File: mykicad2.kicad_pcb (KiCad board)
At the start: 2 copper layers, 8 parts, among them Q1 MMBT3904, Q2 MMBT3906

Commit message: update
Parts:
- added P1: CONN_01X06, Pin_Headers:Pin_Header_Angled_1x06, F.Cu at (170.2, 92.7)
- moved R1 13.1 mm to (143.5, 95.2), turned to 270 degrees
- moved R2 9.16 mm to (143.5, 113.0)
- moved Q1 7.73 mm to (158.8, 95.2), turned to 0 degrees
- moved R3 5.24 mm to (160.0, 102.9), turned to 270 degrees
- moved R4 4.02 mm to (160.0, 108.0), turned to 270 degrees
- turned D1 to 270 degrees
- turned D2 to 270 degrees
- turned Q2 to 0 degrees

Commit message: vertical header pins
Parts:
- P1: footprint Pin_Headers:Pin_Header_Angled_1x06 -> Pin_Headers:Pin_Header_Straight_1x06
- moved D1 6.35 mm to (149.9, 101.6)
- moved D2 6.35 mm to (149.9, 108.0)
- moved R1 6.35 mm to (149.9, 95.2)
- moved R2 6.35 mm to (149.9, 113.0)
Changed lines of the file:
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@@
   )
   (module Diodes_SMD:MiniMELF_Standard (layer F.Cu)
-    (at 143.51 101.6 270)
+    (at 149.86 101.6 270)
     (descr "Diode Mini-MELF Standard")
     (tags "Diode Mini-MELF Standard")
@@
   )
   (module Diodes_SMD:MiniMELF_Standard (layer F.Cu)
-    (at 143.51 107.95 270)
+    (at 149.86 107.95 270)
     (descr "Diode Mini-MELF Standard")
     (tags "Diode Mini-MELF Standard")
@@
   )
   (module Resistors_SMD:R_0603 (layer F.Cu)
-    (at 143.51 95.25 270)
+    (at 149.86 95.25 270)
     (descr "Resistor SMD 0603, reflow soldering, Vishay (see dcrcw.pdf)")
     (tags "resistor 0603")
@@
   )
   (module Resistors_SMD:R_0603 (layer F.Cu)
-    (at 143.51 113.03 270)
+    (at 149.86 113.03 270)
     (descr "Resistor SMD 0603, reflow soldering, Vishay (see dcrcw.pdf)")
     (tags "resistor 0603")
@@
     )
   )
-  (module Pin_Headers:Pin_Header_Angled_1x06 (layer F.Cu)
+  (module Pin_Headers:Pin_Header_Straight_1x06 (layer F.Cu)
     (at 170.18 92.71)
     (descr "Through hole pin header")
@@
       (effects (font (size 1 1) (thickness 0.15)))
     )
-    (fp_line (start -1.5 -1.75) (end -1.5 14.45) (layer F.CrtYd) (width 0.05))
-    (fp_line (start 10.65 -1.75) (end 10.65 14.45) (layer F.CrtYd) (width 0.05))
-    (fp_line (start -1.5 -1.75) (end 10.65 -1.75) (layer F.CrtYd) (width 0.05))
-    (fp_line (start -1.5 14.45) (end 10.65 14.45) (layer F.CrtYd) (width 0.05))
-    (fp_line (start -1.3 -1.55) (end -1.3 0) (layer F.SilkS) (width 0.15))
-    (fp_line (start 0 -1.55) (end -1.3 -1.55) (layer F.SilkS) (width 0.15))
-    (fp_line (start 4.191 -0.127) (end 10.033 -0.127) (layer F.SilkS) (width 0.15))
-    (fp_line (start 10.033 -0.127) (end 10.033 0.127) (layer F.SilkS) (width 0.15))
-    (fp_line (start 10.033 0.127) (end 4.191 0.127) (layer F.SilkS) (width 0.15))
-    (fp_line (start 4.191 0.127) (end 4.191 0) (layer F.SilkS) (width 0.15))
-    (fp_line (start 4.191 0) (end 10.033 0) (layer F.SilkS) (width 0.15))
-    (fp_line (start 1.524 -0.254) (end 1.143 -0.254) (layer F.SilkS) (width 0.15))
-    (fp_line (start 1.524 0.254) (end 1.143 0.254) (layer F.SilkS) (width 0.15))
-    (fp_line (start 1.524 2.286) (end 1.143 2.286) (layer F.SilkS) (width 0.15))
-    (fp_line (start 1.524 2.794) (end 1.143 2.794) (layer F.SilkS) (width 0.15))
-    (fp_line (start 1.524 4.826) (end 1.143 4.826) (layer F.SilkS) (width 0.15))
-    (fp_line (start 1.524 5.334) (end 1.143 5.334) (layer F.SilkS) (width 0.15))
-    (fp_line (start 1.524 12.954) (end 1.143 12.954) (layer F.SilkS) (width 0.15))
-    (fp_line (start 1.524 12.446) (end 1.143 12.446) (layer F.SilkS) (width 0.15))
-    (fp_line (start 1.524 10.414) (end 1.143 10.414) (layer F.SilkS) (width 0.15))
-    (fp_line (start 1.524 9.906) (end 1.143 9.906) (layer F.SilkS) (width 0.15))
-    (fp_line (start 1.524 7.874) (end 1.143 7.874) (layer F.SilkS) (width 0.15))
-    (fp_line (start 1.524 7.366) (end 1.143 7.366) (layer F.SilkS) (width 0.15))
-    (fp_line (start 1.524 -1.27) (end 4.064 -1.27) (layer F.SilkS) (width 0.15))
-    (fp_line (start 1.524 1.27) (end 4.064 1.27) (layer F.SilkS) (width 0.15))
-    (fp_line (start 1.524 1.27) (end 1.524 3.81) (layer F.SilkS) (width 0.15))
-    (fp_line (start 1.524 3.81) (end 4.064 3.81) (layer F.SilkS) (width 0.15))
-    (fp_line (start 4.064 2.286) (end 10.16 2.286) (layer F.SilkS) (width 0.15))
-    (fp_line (start 10.16 2.286) (end 10.16 2.794) (layer F.SilkS) (width 0.15))
-    (fp_line (start 10.16 2.794) (end 4.064 2.794) (layer F.SilkS) (width 0.15))
-    (fp_line (start 4.064 3.81) (end 4.064 1.27) (layer F.SilkS) (width 0.15))
-    (fp_line (start 4.064 1.27) (end 4.064 -1.27) (layer F.SilkS) (width 0.15))
-    (fp_line (start 10.16 0.254) (end 4.064 0.254) (layer F.SilkS) (width 0.15))
-    (fp_line (start 10.16 -0.254) (end 10.16 0.254) (layer F.SilkS) (width 0.15))
-    (fp_line (start 4.064 -0.254) (end 10.16 -0.254) (layer F.SilkS) (width 0.15))
-    (fp_line (start 1.524 1.27) (end 4.064 1.27) (layer F.SilkS) (width 0.15))
-    (fp_line (start 1.524 -1.27) (end 1.524 1.27) (layer F.SilkS) (width 0.15))
-    (fp_line (start 1.524 8.89) (end 4.064 8.89) (layer F.SilkS) (width 0.15))
-    (fp_line (start 1.524 8.89) (end 1.524 11.43) (layer F.SilkS) (width 0.15))
-    (fp_line (start 1.524 11.43) (end 4.064 11.43) (layer F.SilkS) (width 0.15))
-    (fp_line (start 4.064 9.906) (end 10.16 9.906) (layer F.SilkS) (width 0.15))
-    (fp_line (start 10.16 9.906) (end 10.16 10.414) (layer F.SilkS) (width 0.15))
-    (fp_line (start 10.16 10.414) (end 4.064 10.414) (layer F.SilkS) (width 0.15))
-    (fp_line (start 4.064 11.43) (end 4.064 8.89) (layer F.SilkS) (width 0.15))
-    (fp_line (start 4.064 13.97) (end 4.064 11.43) (layer F.SilkS) (width 0.15))
-    (fp_line (start 10.16 12.954) (end 4.064 12.954) (layer F.SilkS) (width 0.15))
-    (fp_line (start 10.16 12.446) (end 10.16 12.954) (layer F.SilkS) (width 0.15))
-    (fp_line (start 4.064 12.446) (end 10.16 12.446) (layer F.SilkS) (width 0.15))
-    (fp_line (start 1.524 13.97) (end 4.064 13.97) (layer F.SilkS) (width 0.15))
-    (fp_line (start 1.524 11.43) (end 1.524 13.97) (layer F.SilkS) (width 0.15))
-    (fp_line (start 1.524 11.43) (end 4.064 11.43) (layer F.SilkS) (width 0.15))
-    (fp_line (start 1.524 6.35) (end 4.064 6.35) (layer F.SilkS) (width 0.15))
-    (fp_line (start 1.524 6.35) (end 1.524 8.89) (layer F.SilkS) (width 0.15))
-    (fp_line (start 1.524 8.89) (end 4.064 8.89) (layer F.SilkS) (width 0.15))
-    (fp_line (start 4.064 7.366) (end 10.16 7.366) (layer F.SilkS) (width 0.15))
-    (fp_line (start 10.16 7.366) (end 10.16 7.874) (layer F.SilkS) (width 0.15))
-    (fp_line (start 10.16 7.874) (end 4.064 7.874) (layer F.SilkS) (width 0.15))
-    (fp_line (start 4.064 8.89) (end 4.064 6.35) (layer F.SilkS) (width 0.15))
-    (fp_line (start 4.064 6.35) (end 4.064 3.81) (layer F.SilkS) (width 0.15))
-    (fp_line (start 10.16 5.334) (end 4.064 5.334) (layer F.SilkS) (width 0.15))
-    (fp_line (start 10.16 4.826) (end 10.16 5.334) (layer F.SilkS) (width 0.15))
-    (fp_line (start 4.064 4.826) (end 10.16 4.826) (layer F.SilkS) (width 0.15))
-    (fp_line (start 1.524 6.35) (end 4.064 6.35) (layer F.SilkS) (width 0.15))
-    (fp_line (start 1.524 3.81) (end 1.524 6.35) (layer F.SilkS) (width 0.15))
-    (fp_line (start 1.524 3.81) (end 4.064 3.81) (layer F.SilkS) (width 0.15))
+    (fp_line (start -1.75 -1.75) (end -1.75 14.45) (layer F.CrtYd) (width 0.05))
+    (fp_line (start 1.75 -1.75) (end 1.75 14.45) (layer F.CrtYd) (width 0.05))
+    (fp_line (start -1.75 -1.75) (end 1.75 -1.75) (layer F.CrtYd) (width 0.05))
+    (fp_line (start -1.75 14.45) (end 1.75 14.45) (layer F.CrtYd) (width 0.05))
+    (fp_line (start 1.27 1.27) (end 1.27 13.97) (layer F.SilkS) (width 0.15))
+    (fp_line (start 1.27 13.97) (end -1.27 13.97) (layer F.SilkS) (width 0.15))
+    (fp_line (start -1.27 13.97) (end -1.27 1.27) (layer F.SilkS) (width 0.15))
+    (fp_line (start 1.55 -1.55) (end 1.55 0) (layer F.SilkS) (width 0.15))
+    (fp_line (start 1.27 1.27) (end -1.27 1.27) (layer F.SilkS) (width 0.15))
+    (fp_line (start -1.55 0) (end -1.55 -1.55) (layer F.SilkS) (width 0.15))
+    (fp_line (start -1.55 -1.55) (end 1.55 -1.55) (layer F.SilkS) (width 0.15))
     (pad 1 thru_hole rect (at 0 0) (size 2.032 1.7272) (drill 1.016) (layers *.Cu *.Mask F.SilkS)
       (net 5 VDD))
@@
     (pad 6 thru_hole oval (at 0 12.7) (size 2.032 1.7272) (drill 1.016) (layers *.Cu *.Mask F.SilkS)
       (net 10 "Net-(P1-Pad6)"))
-    (model Pin_Headers.3dshapes/Pin_Header_Angled_1x06.wrl
+    (model Pin_Headers.3dshapes/Pin_Header_Straight_1x06.wrl
       (at (xyz 0 -0.25 0))
       (scale (xyz 1 1 1))

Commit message: added traces
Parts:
- moved P1 5.08 mm to (170.2, 97.8)
- moved Q2 3.81 mm to (158.8, 113.0)
- moved Q1 1.27 mm to (158.8, 96.5)
- moved R1 1.27 mm to (149.9, 96.5)
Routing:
- net GND: track 0.00 -> 37.1 mm
- net Net-(D1-Pad2): track 0.00 -> 23.4 mm
- net VDD: track 0.00 -> 22.3 mm
- net Net-(D2-Pad2): track 0.00 -> 19.9 mm
- net Net-(P1-Pad4): track 0.00 -> 14.5 mm
- net Net-(D1-Pad1): track 0.00 -> 10.1 mm
- net Net-(Q2-Pad2): track 0.00 -> 6.86 mm
- net Net-(Q1-Pad2): track 0.00 -> 4.73 mm

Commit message: added fill
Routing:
- added copper zone on F.Cu, net GND
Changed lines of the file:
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@@
   (segment (start 160.02 107.2) (end 161.81 105.41) (width 0.25) (layer F.Cu) (net 8) (status 400000))
   (segment (start 161.81 105.41) (end 170.18 105.41) (width 0.25) (layer F.Cu) (net 8) (status 800000))
+  (zone (net 7) (net_name GND) (layer F.Cu) (hatch edge 0.508)
+    (connect_pads (clearance 0.508))
+    (min_thickness 0.254)
+    (fill yes (arc_segments 16) (thermal_gap 0.508) (thermal_bridge_width 0.508))
+    (polygon
+      (pts
+        (xy 144.78 91.44) (xy 175.26 91.44) (xy 175.26 116.84) (xy 144.78 116.84)
+      )
+    )
+  )
 )

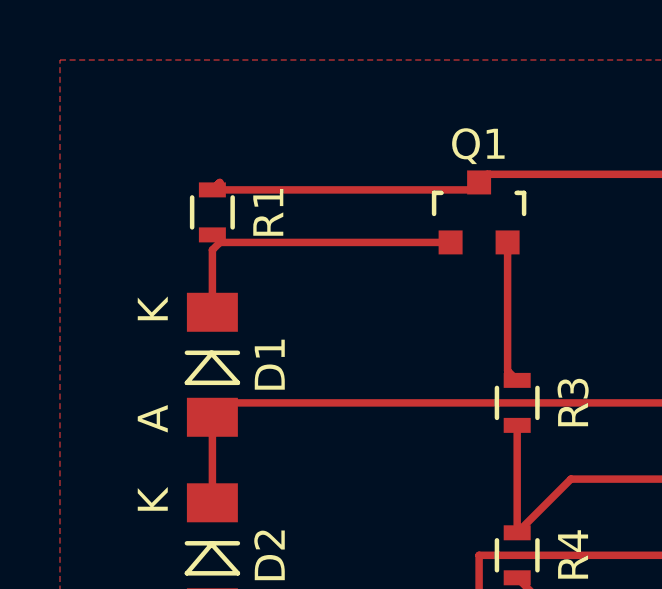
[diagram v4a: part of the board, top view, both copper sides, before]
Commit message: fix trace
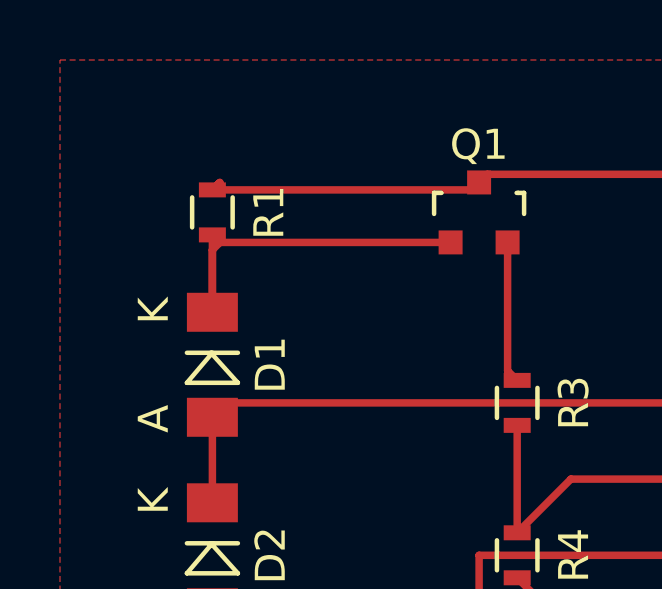
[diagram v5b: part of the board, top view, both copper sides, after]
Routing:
- net Net-(D1-Pad1): track 10.1 -> 12.7 mm
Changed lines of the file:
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@@
   (general
     (links 14)
-    (no_connects 1)
+    (no_connects 0)
     (area 0 0 0 0)
     (thickness 1.6)
     (drawings 0)
-    (tracks 38)
+    (tracks 39)
     (zones 0)
     (modules 9)
@@
     )
   )
+  (segment (start 149.86 97.27) (end 149.86 99.84994) (width 0.25) (layer F.Cu) (net 1) (status C00000))
   (segment (start 157.8 97.52076) (end 150.11076 97.52076) (width 0.25) (layer F.Cu) (net 1) (status 400000))
   (segment (start 149.86 97.77152) (end 149.86 99.84994) (width 0.25) (layer F.Cu) (net 1) (status 800000))

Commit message: improve traces
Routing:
- net GND: track 37.1 -> 46.7 mm
- net Net-(D2-Pad2): track 19.9 -> 11.4 mm
- net Net-(D1-Pad1): track 12.7 -> 10.1 mm
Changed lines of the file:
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@@
   (general
     (links 14)
-    (no_connects 0)
-    (area 0 0 0 0)
+    (no_connects 1)
+    (area 144.78 91.565 175.288334 116.305)
     (thickness 1.6)
     (drawings 0)
-    (tracks 39)
+    (tracks 38)
     (zones 0)
     (modules 9)
@@
       (outputformat 1)
       (mirror false)
-      (drillshape 1)
+      (drillshape 0)
       (scaleselection 1)
-      (outputdirectory ""))
+      (outputdirectory gerber))
   )
   (net 0 "")
@@
     )
   )
-  (segment (start 149.86 97.27) (end 149.86 99.84994) (width 0.25) (layer F.Cu) (net 1) (status C00000))
-  (segment (start 157.8 97.52076) (end 150.11076 97.52076) (width 0.25) (layer F.Cu) (net 1) (status 400000))
-  (segment (start 149.86 97.77152) (end 149.86 99.84994) (width 0.25) (layer F.Cu) (net 1) (status 800000))
+  (segment (start 157.8 97.52076) (end 150.11076 97.52076) (width 0.25) (layer F.Cu) (net 1))
+  (segment (start 149.86 97.77152) (end 149.86 99.84994) (width 0.25) (layer F.Cu) (net 1))
   (segment (start 150.11076 97.52076) (end 149.86 97.77152) (width 0.25) (layer F.Cu) (net 1))
   (segment (start 170.18 102.87) (end 150.34006 102.87) (width 0.25) (layer F.Cu) (net 2))
   (segment (start 150.34006 102.87) (end 149.86 103.35006) (width 0.25) (layer F.Cu) (net 2))
   (segment (start 149.86 103.35006) (end 149.86 106.19994) (width 0.25) (layer F.Cu) (net 2))
-  (segment (start 157.8 114.03076) (end 156.47924 114.03076) (width 0.25) (layer F.Cu) (net 3))
-  (segment (start 147.32 111.76) (end 149.37994 109.70006) (width 0.25) (layer F.Cu) (net 3))
-  (segment (start 147.32 114.3) (end 147.32 111.76) (width 0.25) (layer F.Cu) (net 3))
-  (segment (start 148.59 115.57) (end 147.32 114.3) (width 0.25) (layer F.Cu) (net 3))
-  (segment (start 154.94 115.57) (end 148.59 115.57) (width 0.25) (layer F.Cu) (net 3))
-  (segment (start 156.47924 114.03076) (end 154.94 115.57) (width 0.25) (layer F.Cu) (net 3))
+  (segment (start 157.8 114.03076) (end 155.94076 114.03076) (width 0.25) (layer F.Cu) (net 3))
+  (segment (start 154.19 112.28) (end 149.86 112.28) (width 0.25) (layer F.Cu) (net 3))
+  (segment (start 155.94076 114.03076) (end 154.19 112.28) (width 0.25) (layer F.Cu) (net 3))
   (segment (start 149.37994 109.70006) (end 149.37994 111.79994) (width 0.25) (layer F.Cu) (net 3))
   (segment (start 149.37994 111.79994) (end 149.86 112.28) (width 0.25) (layer F.Cu) (net 3))
@@
   (segment (start 150.10822 95.52178) (end 149.86 95.77) (width 0.25) (layer F.Cu) (net 5))
   (segment (start 150.10822 95.52178) (end 149.86 95.77) (width 0.25) (layer F.Cu) (net 5))
-  (segment (start 159.7 114.03076) (end 160.28924 114.03076) (width 0.25) (layer F.Cu) (net 6) (status 400000))
-  (segment (start 161.29 109.97) (end 160.02 108.7) (width 0.25) (layer F.Cu) (net 6) (status 800000))
+  (segment (start 159.7 114.03076) (end 160.28924 114.03076) (width 0.25) (layer F.Cu) (net 6))
+  (segment (start 161.29 109.97) (end 160.02 108.7) (width 0.25) (layer F.Cu) (net 6))
   (segment (start 161.29 113.03) (end 161.29 109.97) (width 0.25) (layer F.Cu) (net 6))
   (segment (start 160.28924 114.03076) (end 161.29 113.03) (width 0.25) (layer F.Cu) (net 6))
-  (segment (start 158.75 112.03178) (end 158.75 107.95) (width 0.25) (layer F.Cu) (net 7) (status 400000))
-  (segment (start 172.72 100.33) (end 170.18 100.33) (width 0.25) (layer F.Cu) (net 7) (status 800000))
+  (segment (start 158.75 112.03178) (end 156.48178 112.03178) (width 0.25) (layer F.Cu) (net 7))
+  (segment (start 147.32 111.24) (end 149.86 113.78) (width 0.25) (layer F.Cu) (net 7))
+  (segment (start 147.32 109.22) (end 147.32 111.24) (width 0.25) (layer F.Cu) (net 7))
+  (segment (start 148.59 107.95) (end 147.32 109.22) (width 0.25) (layer F.Cu) (net 7))
+  (segment (start 152.4 107.95) (end 148.59 107.95) (width 0.25) (layer F.Cu) (net 7))
+  (segment (start 156.48178 112.03178) (end 152.4 107.95) (width 0.25) (layer F.Cu) (net 7))
+  (segment (start 158.75 112.03178) (end 158.75 107.95) (width 0.25) (layer F.Cu) (net 7))
+  (segment (start 172.72 100.33) (end 170.18 100.33) (width 0.25) (layer F.Cu) (net 7))
   (segment (start 172.72 106.68) (end 172.72 100.33) (width 0.25) (layer F.Cu) (net 7))
   (segment (start 168.91 106.68) (end 172.72 106.68) (width 0.25) (layer F.Cu) (net 7))
   (segment (start 167.64 107.95) (end 168.91 106.68) (width 0.25) (layer F.Cu) (net 7))
   (segment (start 158.75 107.95) (end 167.64 107.95) (width 0.25) (layer F.Cu) (net 7))
-  (segment (start 149.86 113.78) (end 152.92 113.78) (width 0.25) (layer F.Cu) (net 7) (status 400000))
-  (segment (start 154.66822 112.03178) (end 158.75 112.03178) (width 0.25) (layer F.Cu) (net 7) (status 800000))
-  (segment (start 152.92 113.78) (end 154.66822 112.03178) (width 0.25) (layer F.Cu) (net 7))
-  (segment (start 160.02 103.62) (end 160.02 107.2) (width 0.25) (layer F.Cu) (net 8) (status C00000))
-  (segment (start 160.02 107.2) (end 161.81 105.41) (width 0.25) (layer F.Cu) (net 8) (status 400000))
-  (segment (start 161.81 105.41) (end 170.18 105.41) (width 0.25) (layer F.Cu) (net 8) (status 800000))
+  (segment (start 160.02 103.62) (end 160.02 107.2) (width 0.25) (layer F.Cu) (net 8))
+  (segment (start 160.02 107.2) (end 161.81 105.41) (width 0.25) (layer F.Cu) (net 8))
+  (segment (start 161.81 105.41) (end 170.18 105.41) (width 0.25) (layer F.Cu) (net 8))
   (zone (net 7) (net_name GND) (layer F.Cu) (hatch edge 0.508)
     (connect_pads (clearance 0.508))
@@
     (polygon
       (pts
-        (xy 144.78 91.44) (xy 175.26 91.44) (xy 175.26 116.84) (xy 144.78 116.84)
+        (xy 144.78 92.71) (xy 175.26 92.71) (xy 175.26 115.57) (xy 144.78 115.57)
       )
     )

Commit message: big current
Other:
- net class bigcurrent added: clearance 0.2, trace_width 0.5, via_dia 0.7, via_drill 0.4
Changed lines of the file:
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@@
     (uvia_drill 0.1)
     (add_net GND)
-    (add_net "Net-(D1-Pad1)")
-    (add_net "Net-(D1-Pad2)")
-    (add_net "Net-(D2-Pad2)")
-    (add_net "Net-(P1-Pad4)")
     (add_net "Net-(P1-Pad5)")
     (add_net "Net-(P1-Pad6)")
@@
     (add_net "Net-(Q2-Pad2)")
     (add_net VDD)
+  )
+  (net_class bigcurrent ""
+    (clearance 0.2)
+    (trace_width 0.5)
+    (via_dia 0.7)
+    (via_drill 0.4)
+    (uvia_dia 0.3)
+    (uvia_drill 0.1)
+    (add_net "Net-(D1-Pad1)")
+    (add_net "Net-(D1-Pad2)")
+    (add_net "Net-(D2-Pad2)")
+    (add_net "Net-(P1-Pad4)")
   )
   (module TO_SOT_Packages_SMD:SOT-23 (layer F.Cu)
@@
     )
   )
-  (segment (start 157.8 97.52076) (end 150.11076 97.52076) (width 0.25) (layer F.Cu) (net 1))
-  (segment (start 149.86 97.77152) (end 149.86 99.84994) (width 0.25) (layer F.Cu) (net 1))
-  (segment (start 150.11076 97.52076) (end 149.86 97.77152) (width 0.25) (layer F.Cu) (net 1))
-  (segment (start 170.18 102.87) (end 150.34006 102.87) (width 0.25) (layer F.Cu) (net 2))
-  (segment (start 150.34006 102.87) (end 149.86 103.35006) (width 0.25) (layer F.Cu) (net 2))
-  (segment (start 149.86 103.35006) (end 149.86 106.19994) (width 0.25) (layer F.Cu) (net 2))
-  (segment (start 157.8 114.03076) (end 155.94076 114.03076) (width 0.25) (layer F.Cu) (net 3))
-  (segment (start 154.19 112.28) (end 149.86 112.28) (width 0.25) (layer F.Cu) (net 3))
-  (segment (start 155.94076 114.03076) (end 154.19 112.28) (width 0.25) (layer F.Cu) (net 3))
-  (segment (start 149.37994 109.70006) (end 149.37994 111.79994) (width 0.25) (layer F.Cu) (net 3))
-  (segment (start 149.37994 111.79994) (end 149.86 112.28) (width 0.25) (layer F.Cu) (net 3))
+  (segment (start 157.8 97.52076) (end 150.11076 97.52076) (width 0.5) (layer F.Cu) (net 1))
+  (segment (start 149.86 97.77152) (end 149.86 99.84994) (width 0.5) (layer F.Cu) (net 1))
+  (segment (start 150.11076 97.52076) (end 149.86 97.77152) (width 0.5) (layer F.Cu) (net 1))
+  (segment (start 170.18 102.87) (end 150.34006 102.87) (width 0.5) (layer F.Cu) (net 2))
+  (segment (start 150.34006 102.87) (end 149.86 103.35006) (width 0.5) (layer F.Cu) (net 2))
+  (segment (start 149.86 103.35006) (end 149.86 106.19994) (width 0.5) (layer F.Cu) (net 2))
+  (segment (start 157.8 114.03076) (end 155.94076 114.03076) (width 0.5) (layer F.Cu) (net 3))
+  (segment (start 154.19 112.28) (end 149.86 112.28) (width 0.5) (layer F.Cu) (net 3))
+  (segment (start 155.94076 114.03076) (end 154.19 112.28) (width 0.5) (layer F.Cu) (net 3))
+  (segment (start 149.37994 109.70006) (end 149.37994 111.79994) (width 0.5) (layer F.Cu) (net 3))
+  (segment (start 149.37994 111.79994) (end 149.86 112.28) (width 0.5) (layer F.Cu) (net 3))
   (segment (start 159.7 97.52076) (end 159.7 101.8) (width 0.25) (layer F.Cu) (net 4))
   (segment (start 159.7 101.8) (end 160.02 102.12) (width 0.25) (layer F.Cu) (net 4))
@@
   (segment (start 167.64 107.95) (end 168.91 106.68) (width 0.25) (layer F.Cu) (net 7))
   (segment (start 158.75 107.95) (end 167.64 107.95) (width 0.25) (layer F.Cu) (net 7))
-  (segment (start 160.02 103.62) (end 160.02 107.2) (width 0.25) (layer F.Cu) (net 8))
-  (segment (start 160.02 107.2) (end 161.81 105.41) (width 0.25) (layer F.Cu) (net 8))
-  (segment (start 161.81 105.41) (end 170.18 105.41) (width 0.25) (layer F.Cu) (net 8))
+  (segment (start 160.02 103.62) (end 160.02 107.2) (width 0.5) (layer F.Cu) (net 8))
+  (segment (start 160.02 107.2) (end 161.81 105.41) (width 0.5) (layer F.Cu) (net 8))
+  (segment (start 161.81 105.41) (end 170.18 105.41) (width 0.5) (layer F.Cu) (net 8))
   (zone (net 7) (net_name GND) (layer F.Cu) (hatch edge 0.508)
     (connect_pads (clearance 0.508))
